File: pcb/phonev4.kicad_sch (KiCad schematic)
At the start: 38 parts, among them J1 coin, J2 keypad, J3 display, J4 RJ9, J5 mic, J6 card_reader, J7 speaker, Q1 Si2319CDS, U2 TDA2822M

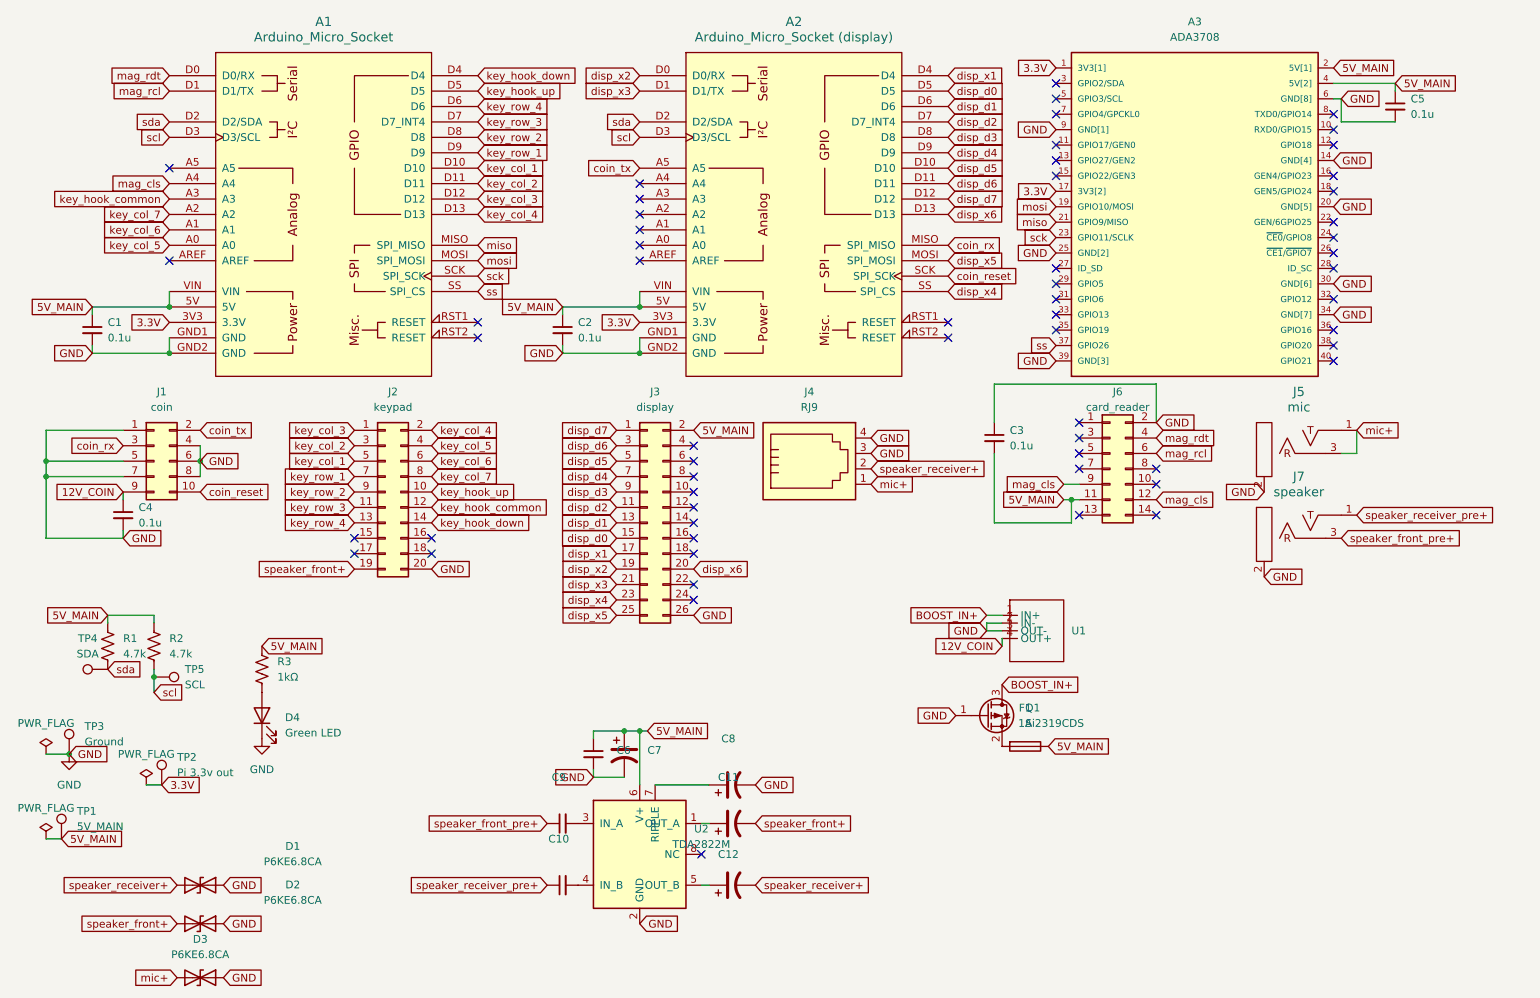
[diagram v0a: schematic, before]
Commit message: pcb: phonev4 KiCad design with project footprint libraries
- Add project-local footprint libs: ADA3708, audio, PCM_arduino-library, misc_footprints
- Q1 THT: TO-220-3_Vertical_GSD for IRF9540N
- R4, R5: 1k for Pi→Arduino reset (unconnected in schematic)
- Updated fp-lib-table, BOM, README, audit script

Made-with: Cursor
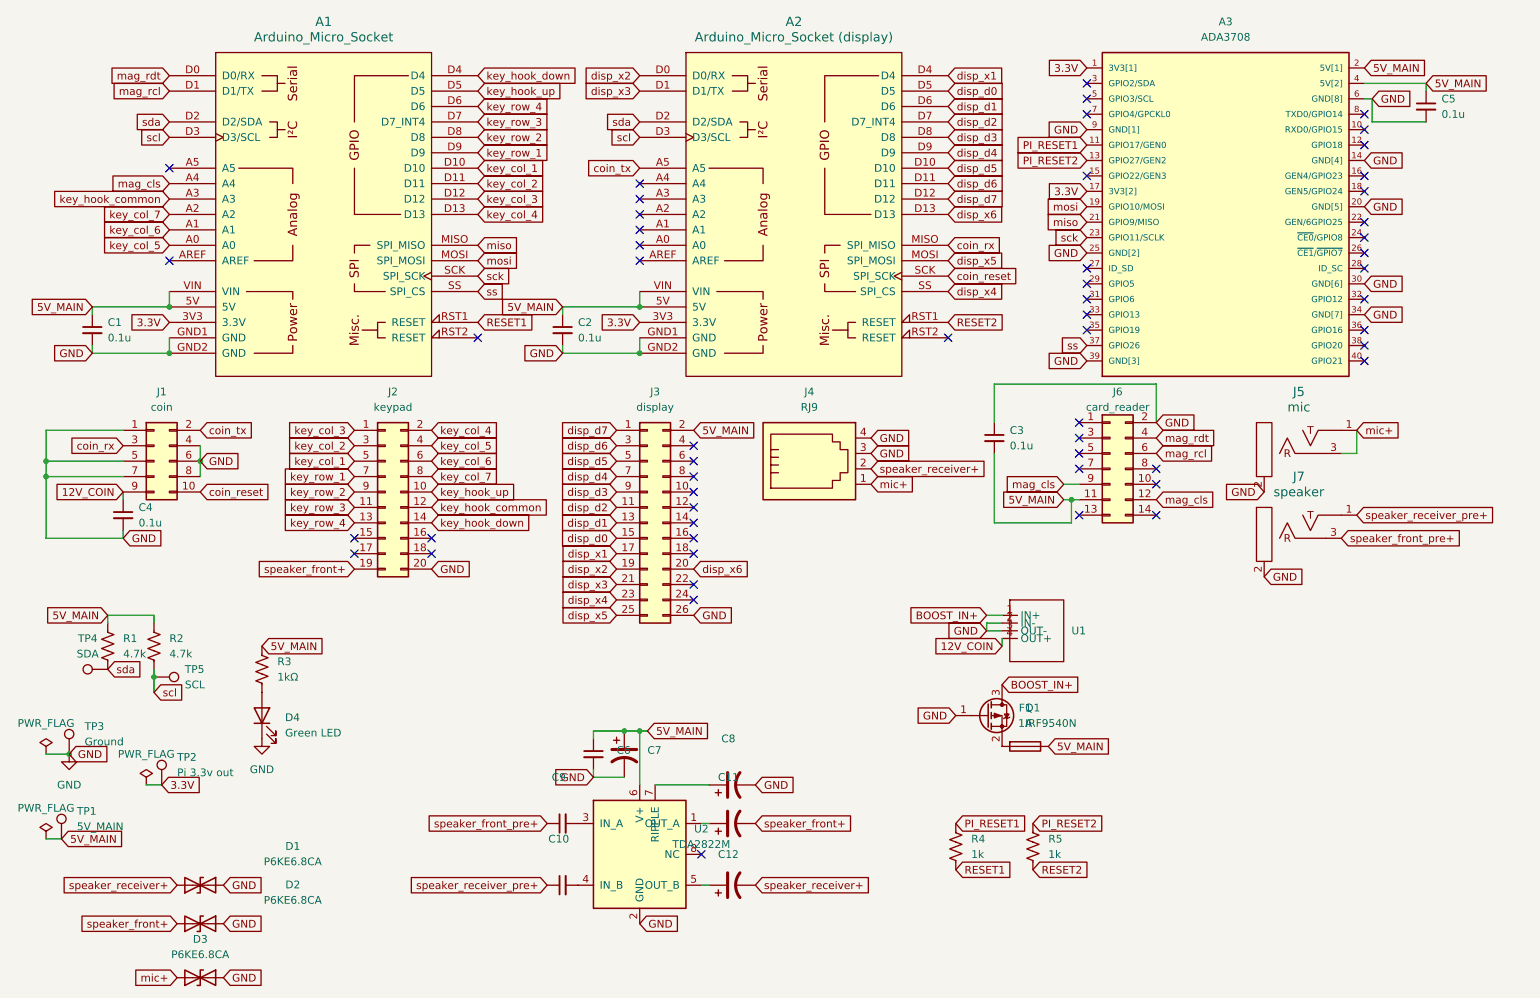
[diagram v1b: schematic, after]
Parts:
- added R4, R5: 1k, Resistor_THT:R_Axial_DIN0204_L3.6mm_D1.6mm_P7.62mm_Horizontal, symbol Device:R_US
- Q1: value Si2319CDS -> IRF9540N; footprint Package_TO_SOT_SMD:SOT-23 -> footprints:TO-220-3_Vertical_GSD; symbol Transistor_FET:Si2319CDS -> phone:IRF9540_THT
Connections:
- net PI_RESET1: now reaches A3.11 (GPIO17/GEN0)
- net PI_RESET1: now also R4.1
- net PI_RESET2: now reaches A3.13 (GPIO27/GEN2)
- net PI_RESET2: now also R5.1
- net RESET2: now reaches A2.RST1 (RESET)
- net RESET2: now also R5.2
- net RESET1: now reaches A1.RST1 (RESET)
- net RESET1: now also R4.2
- no-connect marks 59 -> 55
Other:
- moved on the sheet: A3, C5
